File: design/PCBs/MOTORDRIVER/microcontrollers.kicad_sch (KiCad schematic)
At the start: 20 parts, among them IC1 ATSAME53J18A-MF

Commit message: worked on power and merged programmer and microcontroller sheets
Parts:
- removed ERROR, POWER, PROCESS: LED, symbol Device:LED
- removed R21, R22, R23: R, symbol Device:R
- added 100nF29: C, symbol Device:C
- added U11: ATSAMD11D14A-M, Package_DFN_QFN:QFN-24-1EP_4x4mm_P0.5mm_EP2.6x2.6mm, symbol MCU_Microchip_SAMD:ATSAMD11D14A-M
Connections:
- net +3.3V: now also 100nF29.2, U11.24 (VDD)
- net GND: now also 100nF29.1, U11.23 (GND)
- net SWCLK: no longer names the net of IC1.57 (PA30)
- net SWCLK: now also U11.19 (PA30/SWCLK)
- net SWDIO: no longer names the net of IC1.58 (PA31)
- net SWDIO: now also U11.20 (PA31/SWDIO)
- new net D+: U11.22 (PA25)
- new net D-: U11.21 (PA24)
- no-connect marks 0 -> 18
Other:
- note added: "Decoupling capacitors, place them close to IC"
- note added: "led indicators here?"
- note added: "switch reset button could be nice or not idk"
- note removed: "Decoupling capacitors"
- note removed: "to programmer"

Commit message: added back LED
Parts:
- added D24, D25, D26: LED, symbol Device:LED
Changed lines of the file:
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@@
+	)
+	(symbol
+		(lib_id "Device:LED")
+		(at 74.93 148.59 0)
+		(unit 1)
+		(exclude_from_sim no)
+		(in_bom yes)
+		(on_board yes)
+		(dnp no)
+		(fields_autoplaced yes)
+		(property "Reference" "D26"
+			(at 73.3425 142.24 0)
+			(effects
+				(font
+					(size 1.27 1.27)
+				)
+			)
+		)
+		(property "Value" "LED"
+			(at 73.3425 144.78 0)
+			(effects
+				(font
+					(size 1.27 1.27)
+				)
+			)
+		)
+		(property "Footprint" ""
+			(at 74.93 148.59 0)
+			(effects
+				(font
+					(size 1.27 1.27)
+				)
+				(hide yes)
+			)
+		)
+		(property "Datasheet" "~"
+			(at 74.93 148.59 0)
+			(effects
+				(font
+					(size 1.27 1.27)
+				)
+				(hide yes)
+			)
+		)
+		(property "Description" "Light emitting diode"
+			(at 74.93 148.59 0)
+			(effects
+				(font
+					(size 1.27 1.27)
+				)
+				(hide yes)
+			)
+		)
+		(pin "1"
+		)
+		(pin "2"
+		)
+		(instances
+			(project "motordriver"
+				(path "/c7634e88-16d1-45ec-9aac-9c841e03cf6d/9ebbb593-eaf1-4a56-ba2a-164e20b1d55e"
+					(reference "D26")
+					(unit 1)
+				)
+			)
+		)
 	)
 	(symbol
@@
 	)
 	(symbol
+		(lib_id "Device:LED")
+		(at 74.93 134.62 0)
+		(unit 1)
+		(exclude_from_sim no)
+		(in_bom yes)
+		(on_board yes)
+		(dnp no)
+		(fields_autoplaced yes)
+		(property "Reference" "D25"
+			(at 73.3425 128.27 0)
+			(effects
+				(font
+					(size 1.27 1.27)
+				)
+			)
+		)
+		(property "Value" "LED"
+			(at 73.3425 130.81 0)
+			(effects
+				(font
+					(size 1.27 1.27)
+				)
+			)
+		)
+		(property "Footprint" ""
+			(at 74.93 134.62 0)
+			(effects
+				(font
+					(size 1.27 1.27)
+				)
+				(hide yes)
+			)
+		)
+		(property "Datasheet" "~"
+			(at 74.93 134.62 0)
+			(effects
+				(font
+					(size 1.27 1.27)
+				)
+				(hide yes)
+			)
+		)
+		(property "Description" "Light emitting diode"
+			(at 74.93 134.62 0)
+			(effects
+				(font
+					(size 1.27 1.27)
+				)
+				(hide yes)
+			)
+		)
+		(pin "1"
+		)
+		(pin "2"
+		)
+		(instances
+			(project "motordriver"
+				(path "/c7634e88-16d1-45ec-9aac-9c841e03cf6d/9ebbb593-eaf1-4a56-ba2a-164e20b1d55e"
+					(reference "D25")
+					(unit 1)
+				)
+			)
+		)
+	)
+	(symbol
 		(lib_id "power:+3.3V")
 		(at 76.2 50.8 0)
@@
 					(unit 1)
 				)
+			)
+		)
+	)
+	(symbol
+		(lib_id "Device:LED")
+		(at 74.93 123.19 0)
+		(unit 1)
+		(exclude_from_sim no)
+		(in_bom yes)
+		(on_board yes)
+		(dnp no)
+		(fields_autoplaced yes)
+		(property "Reference" "D24"
+			(at 73.3425 116.84 0)
+			(effects
+				(font
+					(size 1.27 1.27)
+				)
+			)
+		)
+		(property "Value" "LED"
+			(at 73.3425 119.38 0)
+			(effects
+				(font
+					(size 1.27 1.27)
+				)
+			)
+		)
+		(property "Footprint" ""
+			(at 74.93 123.19 0)
+			(effects
+				(font
+					(size 1.27 1.27)
+				)
+				(hide yes)
+			)
+		)
+		(property "Datasheet" "~"
+			(at 74.93 123.19 0)
+			(effects
+				(font
+					(size 1.27 1.27)
+				)
+				(hide yes)
+			)
+		)
+		(property "Description" "Light emitting diode"
+			(at 74.93 123.19 0)
+			(effects
+				(font
+					(size 1.27 1.27)
+				)
+				(hide yes)
+			)
+		)
+		(pin "1"
+		)
+		(pin "2"
+		)
+		(instances
+			(project ""
+				(path "/c7634e88-16d1-45ec-9aac-9c841e03cf6d/9ebbb593-eaf1-4a56-ba2a-164e20b1d55e"
+					(reference "D24")
+					(unit 1)
+				)

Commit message: finished 12v voltage, The components for alost all ICs need values. Cleaned up a bit
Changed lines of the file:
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@@
 	(text "switch reset button could be nice\nor not idk\n"
 		(exclude_from_sim no)
-		(at 212.852 77.47 0)
+		(at 225.806 63.5 0)
 		(effects
 			(font

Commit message: Removed unneccessary TMC4761 pins
Finally went through every pin on the TMC and tried to eliminate
unneeded pins. Reduced sheet complexity quite nicely. Pretty much
all rationales for removing pins were added to the design document,
although not formatted that nicely yet.
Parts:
- renumbered 100nF29 to 100nF
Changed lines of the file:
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@@
 		(on_board yes)
 		(dnp no)
-		(property "Reference" "100nF29"
-			(at 251.333 45.593 90)
+		(property "Reference" "100nF"
+			(at 250.698 58.674 90)
 			(effects
 				(font
@@
 			(project "motordriver"
 				(path "/c7634e88-16d1-45ec-9aac-9c841e03cf6d/9ebbb593-eaf1-4a56-ba2a-164e20b1d55e"
-					(reference "100nF29")
+					(reference "100nF")
 					(unit 1)
 				)

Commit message: Switched TMC hall sensor input to digital from motors
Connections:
- net driverIC2_CS: now reaches IC1.39 (PB16)
- net driverIC1_CS: now reaches IC1.40 (PB17)
- net driverIC_CS: now reaches IC1.41 (PA20)
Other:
- note added: "Chip select for different motors"
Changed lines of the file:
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@@
+		)
+	)
+	(text "Chip select for\ndifferent motors\n"
+		(exclude_from_sim no)
+		(at 200.152 109.982 0)
+		(effects
+			(font
+				(size 1.27 1.27)
+			)
 		)
 	)
@@
 		)
 	)
+	(hierarchical_label "driverIC2_CS"
+		(shape input)
+		(at 173.99 113.03 0)
+		(fields_autoplaced yes)
+		(effects
+			(font
+				(size 1.27 1.27)
+			)
+			(justify left)
+		)
+	)
 	(hierarchical_label "SDA IMU1"
 		(shape input)
@@
 		)
 	)
+	(hierarchical_label "driverIC1_CS"
+		(shape input)
+		(at 173.99 110.49 0)
+		(fields_autoplaced yes)
+		(effects
+			(font
+				(size 1.27 1.27)
+			)
+			(justify left)
+		)
+	)
 	(hierarchical_label "D+"
 		(shape input)
@@
 		)
 	)
+	(hierarchical_label "driverIC_CS"
+		(shape input)
+		(at 173.99 107.95 0)
+		(fields_autoplaced yes)
+		(effects
+			(font
+				(size 1.27 1.27)
+			)
+			(justify left)
+		)
+	)

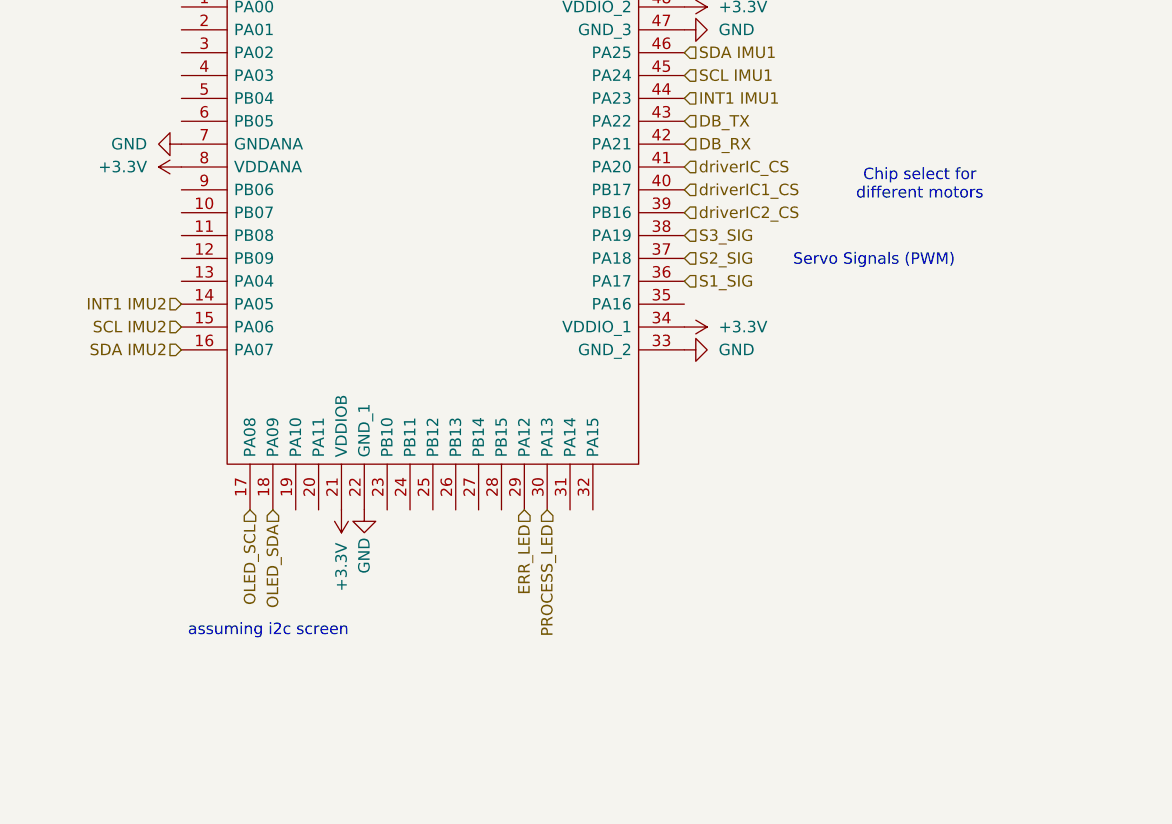
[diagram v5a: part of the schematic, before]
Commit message: TMC and MCU connections
Further progress on PCB. Main remainders are:

Voltage regulator page  (couple todos)
Fix sheet duplication for output sheets
Decide on UART or SPI debug for TMC
Formalize stuff, fill out bottom right on sheets
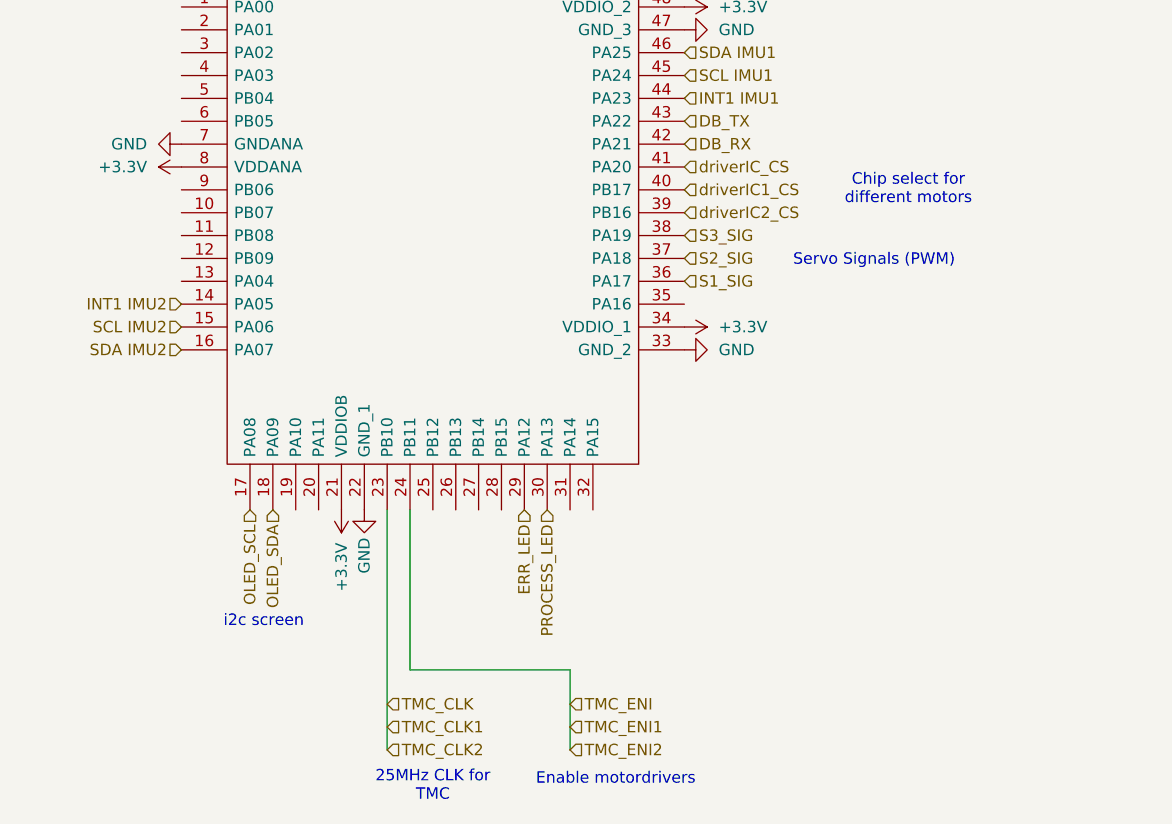
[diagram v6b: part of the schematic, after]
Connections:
- net TMC_CLK: now reaches IC1.23 (PB10)
- net TMC_ENI: now reaches IC1.24 (PB11)
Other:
- note added: "25MHz CLK for TMC"
- note added: "Enable motordrivers"
- note added: "i2c screen"
- note removed: "assuming i2c screen"
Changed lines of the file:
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@@
+	(wire
+		(pts
+			(xy 143.51 163.83) (xy 161.29 163.83)
+		)
+		(stroke
+			(width 0)
+			(type default)
+		)
+	)
 	(wire
 		(pts
@@
 	(wire
 		(pts
+			(xy 143.51 146.05) (xy 143.51 163.83)
+		)
+		(stroke
+			(width 0)
+			(type default)
+		)
+	)
+	(wire
+		(pts
 			(xy 156.21 40.64) (xy 162.56 40.64)
 		)
@@
 	(wire
 		(pts
+			(xy 161.29 163.83) (xy 161.29 172.72)
+		)
+		(stroke
+			(width 0)
+			(type default)
+		)
+	)
+	(wire
+		(pts
 			(xy 156.21 50.8) (xy 156.21 54.61)
 		)
@@
 	(wire
 		(pts
+			(xy 140.97 146.05) (xy 140.97 172.72)
+		)
+		(stroke
+			(width 0)
+			(type default)
+		)
+	)
+	(wire
+		(pts
 			(xy 151.13 62.23) (xy 151.13 69.85)
 		)
@@
 	(text "Chip select for\ndifferent motors\n"
 		(exclude_from_sim no)
-		(at 200.152 109.982 0)
-		(effects
-			(font
-				(size 1.27 1.27)
-			)
-		)
-	)
-	(text "assuming i2c screen"
-		(exclude_from_sim no)
-		(at 127.762 159.512 0)
+		(at 198.882 110.49 0)
+		(effects
+			(font
+				(size 1.27 1.27)
+			)
+		)
+	)
+	(text "i2c screen"
+		(exclude_from_sim no)
+		(at 127.254 158.496 0)
 		(effects
 			(font
@@
 		)
 	)
+	(text "Enable motordrivers"
+		(exclude_from_sim no)
+		(at 166.37 176.022 0)
+		(effects
+			(font
+				(size 1.27 1.27)
+			)
+		)
+	)
+	(text "25MHz CLK for \nTMC"
+		(exclude_from_sim no)
+		(at 146.05 176.784 0)
+		(effects
+			(font
+				(size 1.27 1.27)
+			)
+		)
+	)
 	(text "Decoupling capacitors, place them close to IC"
 		(exclude_from_sim no)
@@
 		)
 	)
+	(hierarchical_label "TMC_CLK1"
+		(shape input)
+		(at 140.97 170.18 0)
+		(fields_autoplaced yes)
+		(effects
+			(font
+				(size 1.27 1.27)
+			)
+			(justify left)
+		)
+	)
 	(hierarchical_label "D+"
 		(shape input)
@@
 		)
 	)
+	(hierarchical_label "TMC_CLK"
+		(shape input)
+		(at 140.97 167.64 0)
+		(fields_autoplaced yes)
+		(effects
+			(font
+				(size 1.27 1.27)
+			)
+			(justify left)
+		)
+	)
 	(hierarchical_label "DB_RX"
 		(shape input)
@@
 		)
 	)
+	(hierarchical_label "TMC_CLK2"
+		(shape input)
+		(at 140.97 172.72 0)
+		(fields_autoplaced yes)
+		(effects
+			(font
+				(size 1.27 1.27)
+			)
+			(justify left)
+		)
+	)
+	(hierarchical_label "TMC_ENI2"
+		(shape input)
+		(at 161.29 172.72 0)
+		(fields_autoplaced yes)
+		(effects
+			(font
+				(size 1.27 1.27)
+			)
+			(justify left)
+		)
+	)
 	(hierarchical_label "SCL IMU2"
 		(shape input)
@@
 		)
 	)
+	(hierarchical_label "TMC_ENI1"
+		(shape input)
+		(at 161.29 170.18 0)
+		(fields_autoplaced yes)
+		(effects
+			(font
+				(size 1.27 1.27)
+			)
+			(justify left)
+		)
+	)
 	(hierarchical_label "SCL IMU1"
 		(shape input)
@@
 		(fields_autoplaced yes)
 		(effects
+			(font
+				(size 1.27 1.27)
+			)
+			(justify left)
+		)
+	)
+	(hierarchical_label "TMC_ENI"
+		(shape input)
+		(at 161.29 167.64 0)
+		(fields_autoplaced yes)
+		(effects
